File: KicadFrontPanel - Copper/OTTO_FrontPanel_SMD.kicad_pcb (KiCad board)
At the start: 2 copper layers, 294.5 x 102.3 mm, 75 parts, among them SW1 ALPS SKHC, SW10 ALPS SKHC, SW11 ALPS SKHC, SW12 ALPS SKHC, SW13 ALPS SKHC, SW14 ALPS SKHC, SW15 ALPS SKHC, SW16 ALPS SKHC, SW17 ALPS SKHC, SW18 ALPS SKHC, SW19 ALPS SKHC, SW2 ALPS SKHC, SW20 ALPS SKHC, SW21 ALPS SKHC, SW22 ALPS SKHC, SW23 ALPS SKHC, SW24 ALPS SKHC, SW25 ALPS SKHC, SW26 ALPS SKHC, SW3 ALPS SKHC, SW32 6x6x13mm, SW33 6x6x13mm, SW38 6x6x13mm, SW4 ALPS SKHC, SW5 ALPS SKHC, SW6 ALPS SKHC, SW7 ALPS SKHC, SW8 ALPS SKHC, SW9 ALPS SKHC

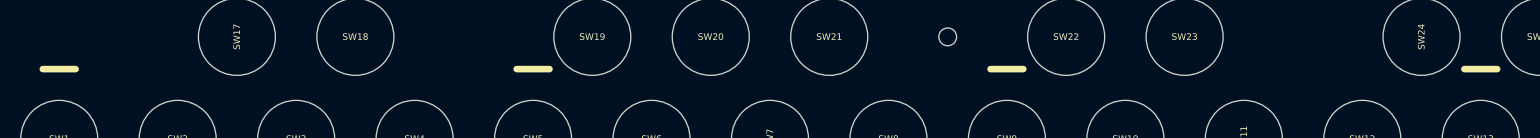
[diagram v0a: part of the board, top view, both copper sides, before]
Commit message: Finished copper version
Rebased copper version on finished non-copper version and finished copper version
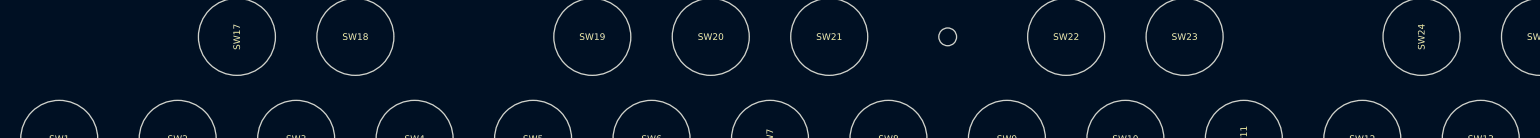
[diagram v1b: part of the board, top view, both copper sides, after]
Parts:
- moved G*** 6.10 mm to (33.5, 31.8)
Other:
- board text added: "HEADPHONES"
- board text added: "LINE IN"
- board text added: "LINE OUT"
- board text added: "MIDI IN"
- board text added: "MIDI OUT"
- board text added: "MIDI THRU"
- board text added: "USB"
